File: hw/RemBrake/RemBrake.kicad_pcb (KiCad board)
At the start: 2 copper layers, 40 x 80 mm, 103 parts, among them IC1 LTC2943IDD#TRPBF, J1 Screw_Terminal_01x02, J2 Conn_01x03_MountingPin, J3 Screw_Terminal_01x04, J4 Conn_01x08_MountingPin, J5 Conn_01x04_MountingPin, J6 Conn_01x03_MountingPin, J7 Conn_01x07, J8 Conn_01x07, J9 Conn_01x03, Q1 SiS415DNT, Q2 BC337, Q3 BC847, Q4 BC337, Q5 BC847, Q6 BC337, Q7 BC847, Q8 BC337, Q9 BC847, U1 TPS62140, U2 BD48ExxG, U3 XC6220B331MR, U4 MAX40200AUK, U5 LM555xN, U6 MAX40200AUK, U7 MAX40200AUK

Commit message: added connector labels
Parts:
- removed REF**: WEEE-Logo_4.2x6mm_SilkScreen, Symbol:WEEE-Logo_4.2x6mm_SilkScreen
- removed REF**: OSHW-Symbol_6.7x6mm_SilkScreen, Symbol:OSHW-Symbol_6.7x6mm_SilkScreen
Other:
- board text added: "+"
- board text added: "BALANCE"
- board text added: "BATTERY"
- board text added: "EXT SENSOR"
- board text added: "G"
- board text added: "GND"
- board text added: "HANDLEBARS"
- board text added: "INDICATOR"
- board text added: "LEDBAR"
- board text added: "ON/OFF"
- board text added: "Pacner Bros Tech"
- board text added: "SERVO"
- board text added: "VBAT"
- board text added: "VOUT"
- board text removed: "Pacner Bros Design"

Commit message: added OH symbol and waste directive
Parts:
- added REF**: OSHW-Symbol_6.7x6mm_SilkScreen, Symbol:OSHW-Symbol_6.7x6mm_SilkScreen, B.Cu at (153.1, 67.7)
- added REF**: WEEE-Logo_4.2x6mm_SilkScreen, Symbol:WEEE-Logo_4.2x6mm_SilkScreen, B.Cu at (153.1, 74.7)

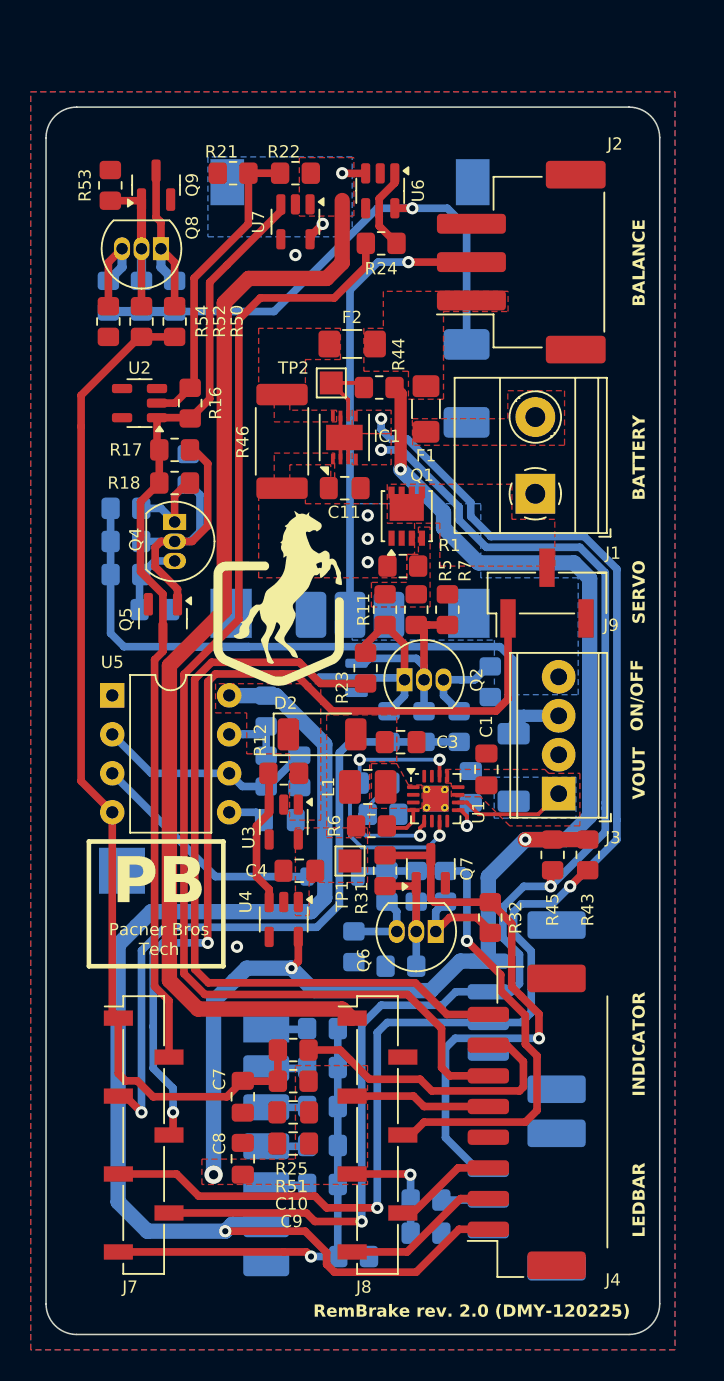
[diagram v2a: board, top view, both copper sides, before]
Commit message: since the name of the repository changed, the paths of the 3d symbols have been changed as well
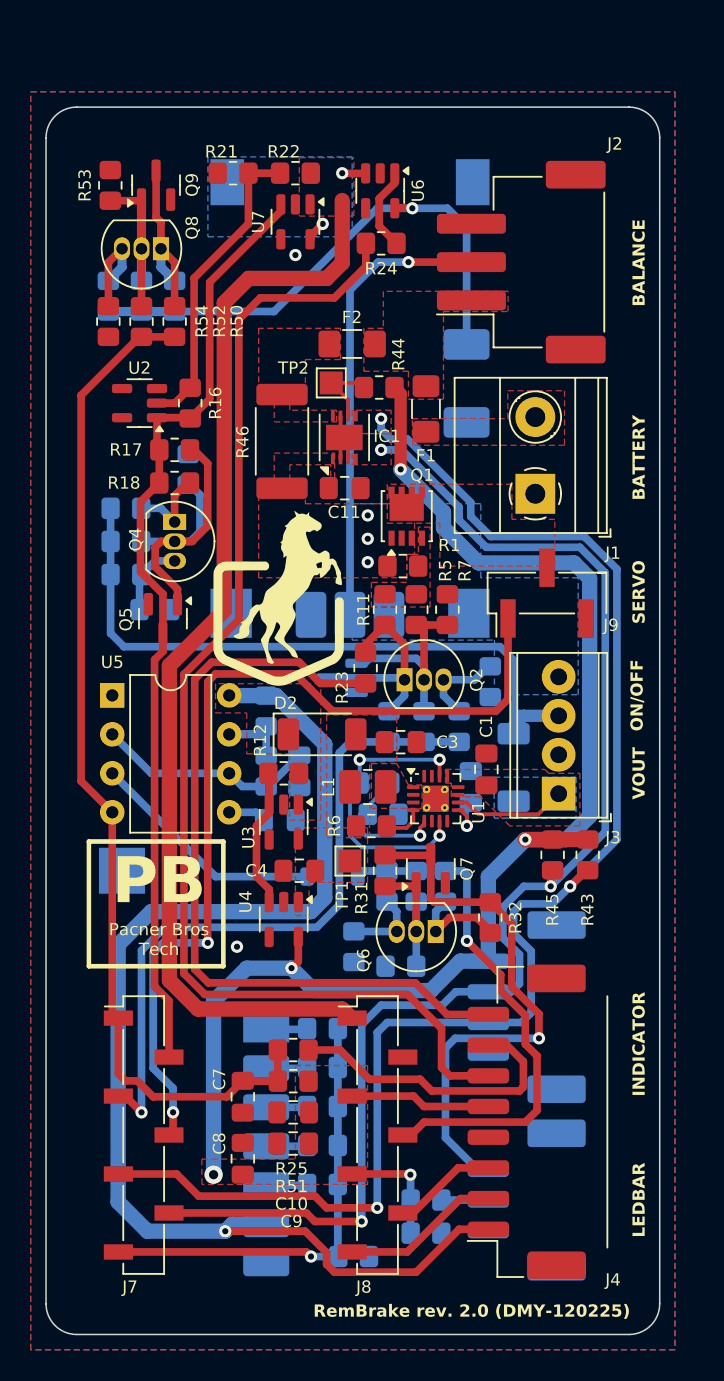
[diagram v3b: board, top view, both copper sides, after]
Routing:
- net /power_switch/ON/OFF: track 46.5 -> 43.1 mm

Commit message: added few components to fix indicator LED undefined cathode voltage and added vbus divider to match MCU voltage level
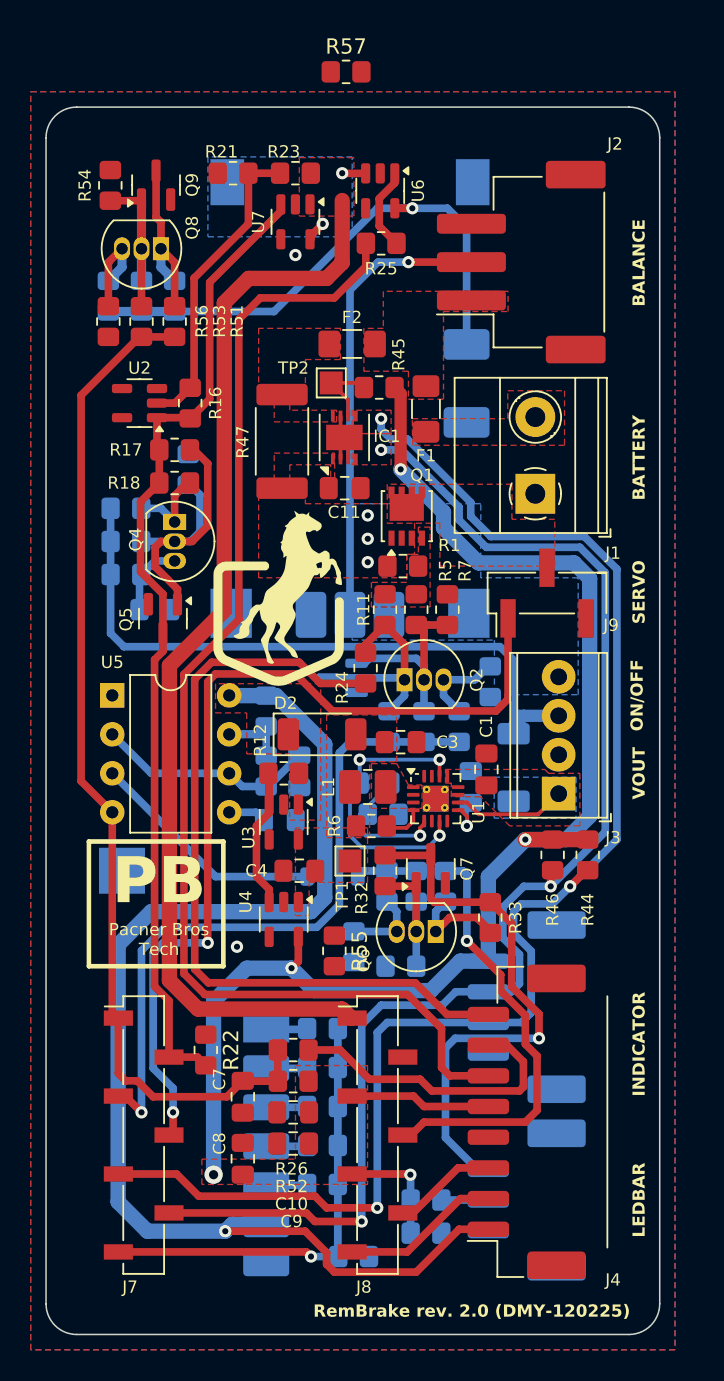
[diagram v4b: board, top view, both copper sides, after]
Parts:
- removed REF**: OSHW-Symbol_6.7x6mm_SilkScreen, Symbol:OSHW-Symbol_6.7x6mm_SilkScreen
- removed REF**: WEEE-Logo_4.2x6mm_SilkScreen, Symbol:WEEE-Logo_4.2x6mm_SilkScreen
- added R22: 10k, Resistor_SMD:R_0805_2012Metric_Pad1.20x1.40mm_HandSolder, F.Cu at (130.4, 121.5)
- added R55: 10k, Resistor_SMD:R_0805_2012Metric_Pad1.20x1.40mm_HandSolder, F.Cu at (138.8, 115.0)
- added R57: 10k, Resistor_SMD:R_0805_2012Metric_Pad1.20x1.40mm_HandSolder, F.Cu at (139.6, 57.7)
- R7: value 4k2 -> 42k
- renumbered R22 to R23, R23 to R24, R24 to R25, R25 to R26, R26 to R27, R27 to R28, R28 to R29, R29 to R30, R30 to R31, R31 to R32, R32 to R33, R33 to R34, R34 to R35, R35 to R36, R36 to R37, R37 to R38, R38 to R39, R39 to R40, R40 to R41, R41 to R42, R42 to R43, R43 to R44, R44 to R45, R45 to R46, R46 to R47, R47 to R48, R48 to R49, R49 to R50, R50 to R51, R51 to R52, R52 to R53, R53 to R54, R54 to R56
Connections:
- net /brake_control/CHARGING renamed /brake_control/STATUS
- U6 pad 3: Net-(M2-Vin) -> Net-(U6-EN)
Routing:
- net /brake_control/ENABLE: track 62.0 -> 64.7 mm

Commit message: updated routing yet need to do some small adjustment of the polygon priorities
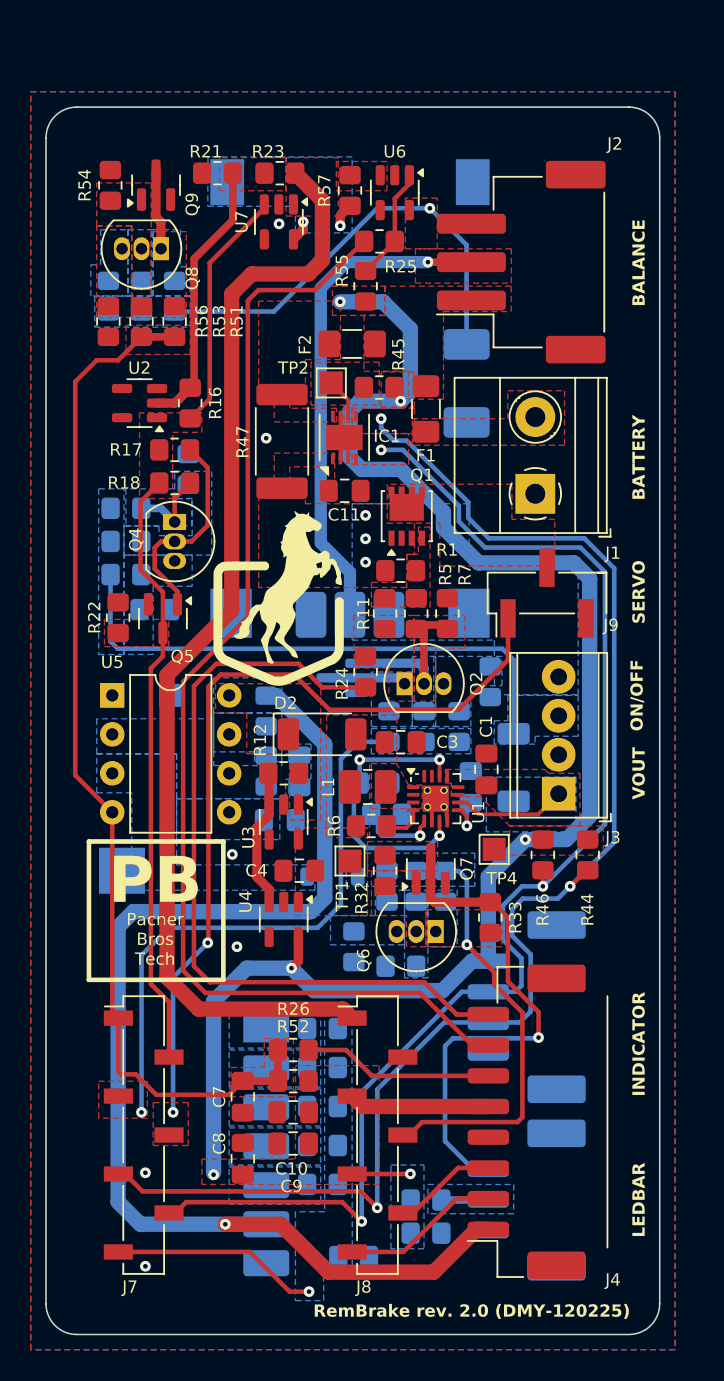
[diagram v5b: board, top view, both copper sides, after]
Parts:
- added REF**: OSHW-Symbol_6.7x6mm_SilkScreen, Symbol:OSHW-Symbol_6.7x6mm_SilkScreen, B.Cu at (153.1, 67.5)
- added REF**: WEEE-Logo_4.2x6mm_SilkScreen, Symbol:WEEE-Logo_4.2x6mm_SilkScreen, B.Cu at (153.1, 74.7)
- added TP3: TestPoint_Probe, TestPoint:TestPoint_Pad_1.5x1.5mm, B.Cu at (128.1, 98.3)
- added TP4: TestPoint_Probe, TestPoint:TestPoint_Pad_1.5x1.5mm, F.Cu at (149.2, 108.4)
- moved R55 43.4 mm to (140.8, 71.7), turned to 90 degrees
- moved R22 28.8 mm to (124.7, 93.3)
- moved R57 7.74 mm to (139.8, 65.4), turned to 90 degrees
- moved U7 1.08 mm to (135.2, 67.5)
- moved R21 1.02 mm to (131.2, 64.3)
- moved R23 1.02 mm to (135.2, 64.3)
- moved U6 0.96 mm to (142.7, 65.6)
- moved R46 0.64 mm to (152.4, 108.7)
- moved R1 0.33 mm to (143.1, 90.2)
- moved R11 0.25 mm to (142.1, 93.0)
- moved R5 0.25 mm to (144.1, 93.0)
- moved R7 0.25 mm to (146.2, 93.0)
- moved Q2 0.25 mm to (143.4, 97.6)
- moved R24 0.25 mm to (140.8, 96.8)
- moved R9 0.23 mm to (142.2, 106.1)
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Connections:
- J4 pad 6: /control_connector/GREEN -> /control_connector/BLUE
- J4 pad 7: /control_connector/BLUE -> /control_connector/GREEN
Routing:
- net /brake_control/RF SWITCH: track 29.3 -> 13.5 mm
- net Net-(D3-A): track 15.5 -> 0.00 mm
- net Net-(U5-THR): track 14.4 -> 0.00 mm
- net Net-(Q8-B): track 11.1 -> 0.00 mm
- net +3V3: track 97.4 -> 108.4 mm, vias 4 -> 5
- net Net-(Q6-B): track 9.46 -> 0.00 mm
- net /brake_control/ENABLE: track 64.7 -> 55.3 mm
- net /control_connector/LED RED: track 14.0 -> 5.16 mm
- net Net-(Q4-B): track 21.4 -> 13.8 mm
- net /brake_control/BUZZ: track 34.0 -> 26.7 mm
- net /control_connector/BLUE: track 19.6 -> 12.4 mm
- net /power_switch/ON/OFF: track 43.1 -> 35.9 mm
- net /brake_control/POWER SW: track 44.6 -> 37.7 mm
- net Net-(Q6-C): track 6.62 -> 0.00 mm
- net Net-(Q8-E): track 6.58 -> 0.00 mm
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- added copper zone on B.Cu, net +5V
- added copper zone on B.Cu, net /brake_control/BTN
- added copper zone on B.Cu, net /brake_control/BUZZ
- added copper zone on F.Cu, net /brake_control/BUZZER
- added copper zone on F.Cu, net /brake_control/ENABLE
- added copper zone on B.Cu, net /brake_control/POWER SW
- added copper zone on F.Cu, net /brake_control/POWER SW
- added copper zone on B.Cu, net /brake_control/RF SWITCH
- added copper zone on F.Cu, net /brake_control/SERVO
- added copper zone on F.Cu, net /brake_control/STATUS
- added copper zone on B.Cu, net /control_connector/BUTTON
- added copper zone on B.Cu, net /control_connector/LED RED
- added copper zone on F.Cu, net /control_connector/LED RED
- added copper zone on F.Cu, net /power_manager/BM
- added copper zone on B.Cu, net /power_switch/ON/OFF
- added copper zone on B.Cu, net Net-(D3-A)
- added copper zone on F.Cu, net Net-(IC1-~{ALCC})
- added copper zone on B.Cu, net Net-(M1-D0)
- added copper zone on B.Cu, net Net-(M1-D1)
- added copper zone on B.Cu, net Net-(M1-D2)
- added copper zone on B.Cu, net Net-(M1-D3)
- added copper zone on B.Cu, net Net-(M1-VT)
- added copper zone on B.Cu, net Net-(M2-LED)
- added copper zone on F.Cu, net Net-(M2-LED)
- added copper zone on B.Cu, net Net-(Q2-B)
- added copper zone on F.Cu, net Net-(Q2-B)
- added copper zone on B.Cu, net Net-(Q2-E)
- added copper zone on B.Cu, net Net-(Q4-B)
- added copper zone on B.Cu, net Net-(Q4-C)
- added copper zone on B.Cu, net Net-(Q4-E)
- added copper zone on B.Cu, net Net-(Q6-B)
- added copper zone on F.Cu, net Net-(Q6-B)
- added copper zone on B.Cu, net Net-(Q6-C)
- added copper zone on F.Cu, net Net-(Q6-C)
- added copper zone on B.Cu, net Net-(Q6-E)
- added copper zone on B.Cu, net Net-(Q8-B)
- added copper zone on F.Cu, net Net-(Q8-B)
- added copper zone on B.Cu, net Net-(Q8-C)
- added copper zone on F.Cu, net Net-(Q8-C)
- added copper zone on B.Cu, net Net-(Q8-E)
- added copper zone on F.Cu, net Net-(Q8-E)
- added copper zone on F.Cu, net Net-(U2-VDD)
- added copper zone on B.Cu, net Net-(U5-CV)
- added copper zone on B.Cu, net Net-(U5-DIS)
- added copper zone on B.Cu, net Net-(U5-THR)
- added copper zone on F.Cu, net Net-(U6-EN)

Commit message: finalized RemBrake version 2
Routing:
- net Net-(Q4-B): track 13.8 -> 14.4 mm
